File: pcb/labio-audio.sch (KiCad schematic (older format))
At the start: 27 parts

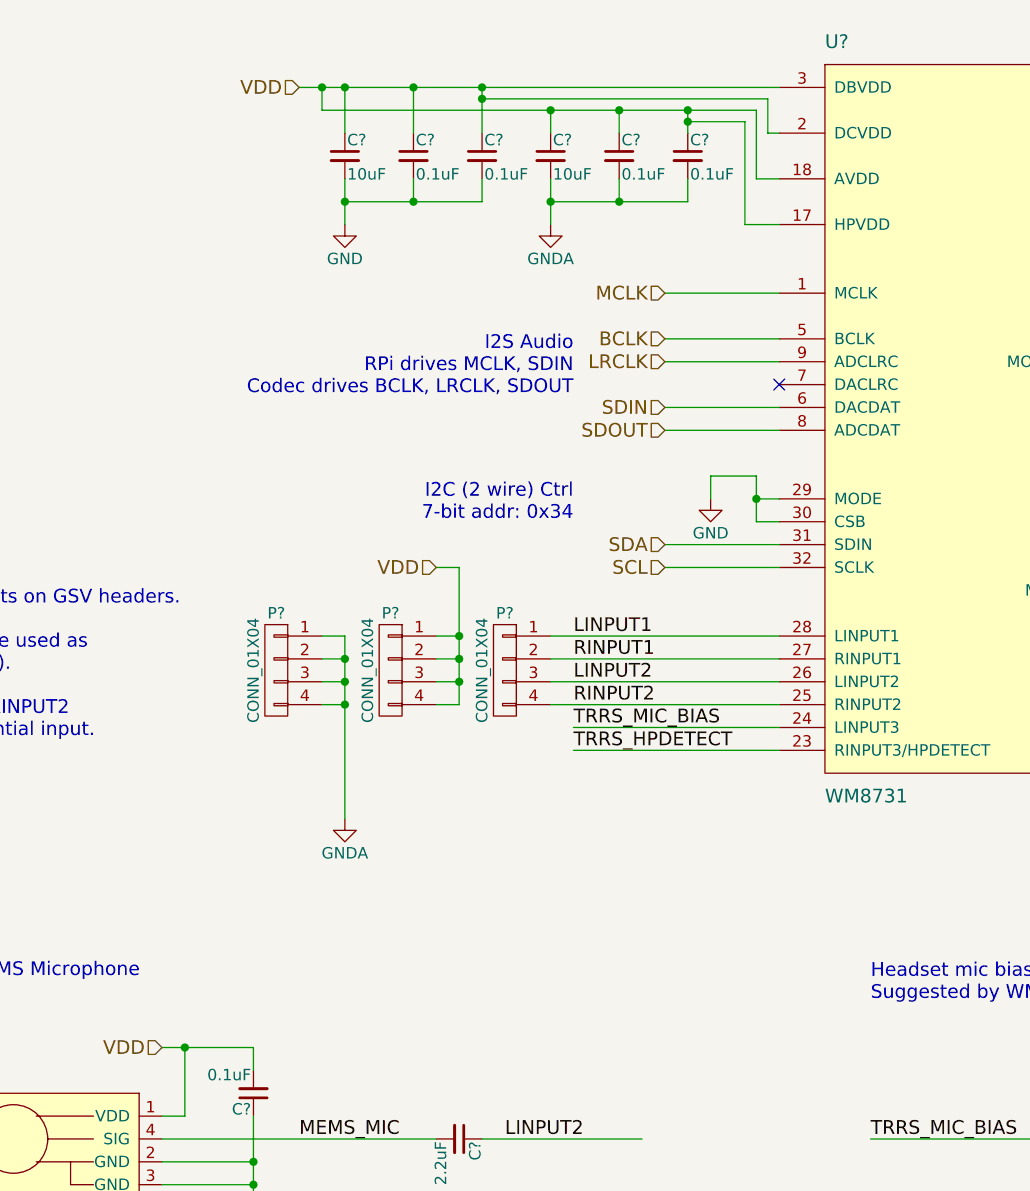
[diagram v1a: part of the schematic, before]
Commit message: add imu sensors, make top level connections
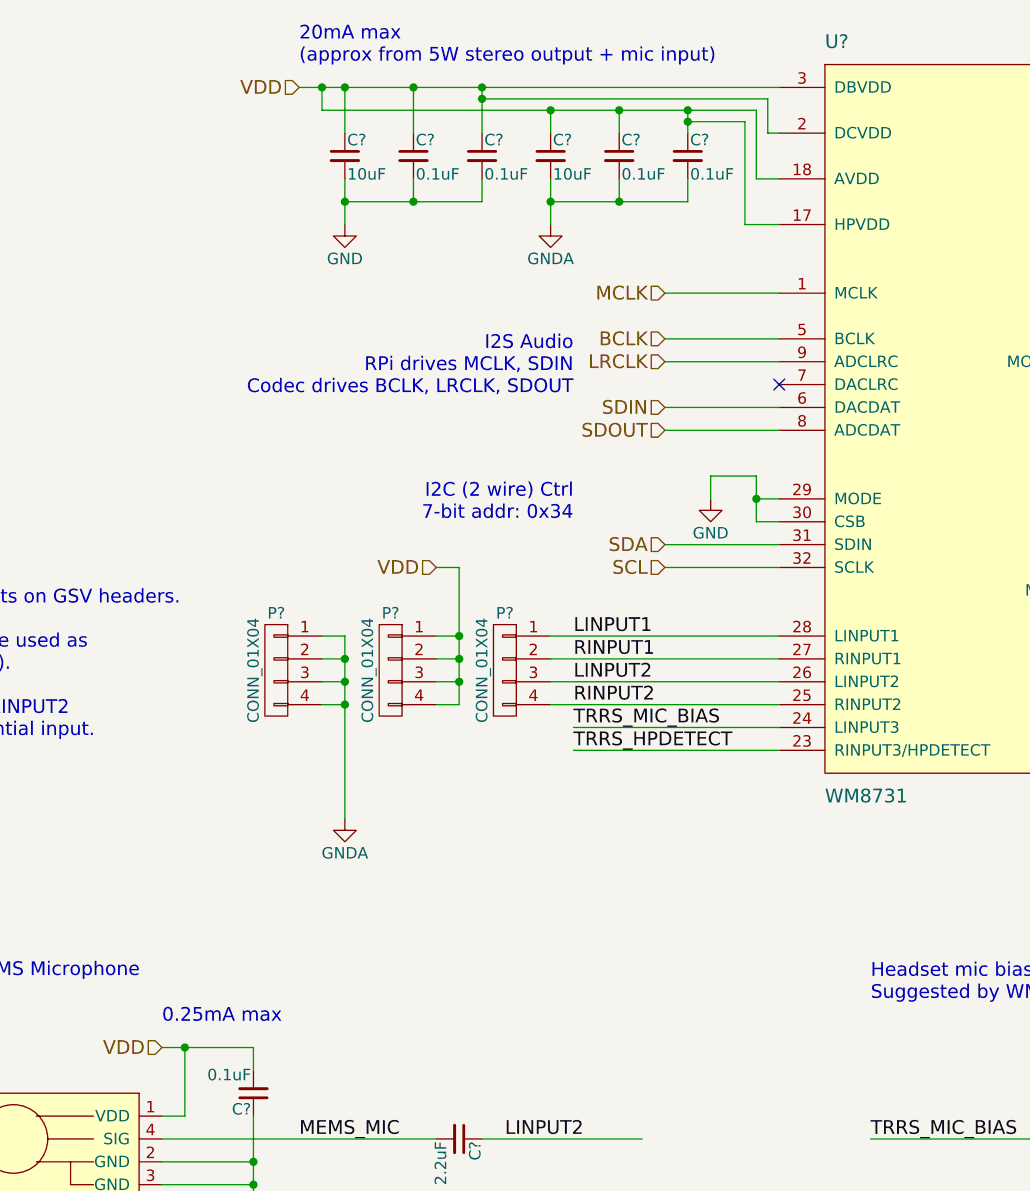
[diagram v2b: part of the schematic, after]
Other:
- note added: "0.25mA max"
- note added: "20mA max\n(approx from 5W stereo output + mic input)"
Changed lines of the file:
@@
 $Descr A4 11693 8268
 encoding utf-8
-Sheet 4 8
+Sheet 4 7
 Title ""
 Date ""
@@
 Text Notes 5700 5000 0    60   ~ 0
 Headset mic bias\nSuggested by WM8750BL datasheet (pg. 56).
+Text Notes 2600 5100 0    60   ~ 0
+0.25mA max
+Text Notes 3200 900  0    60   ~ 0
+20mA max\n(approx from 5W stereo output + mic input)
 $EndSCHEMATC

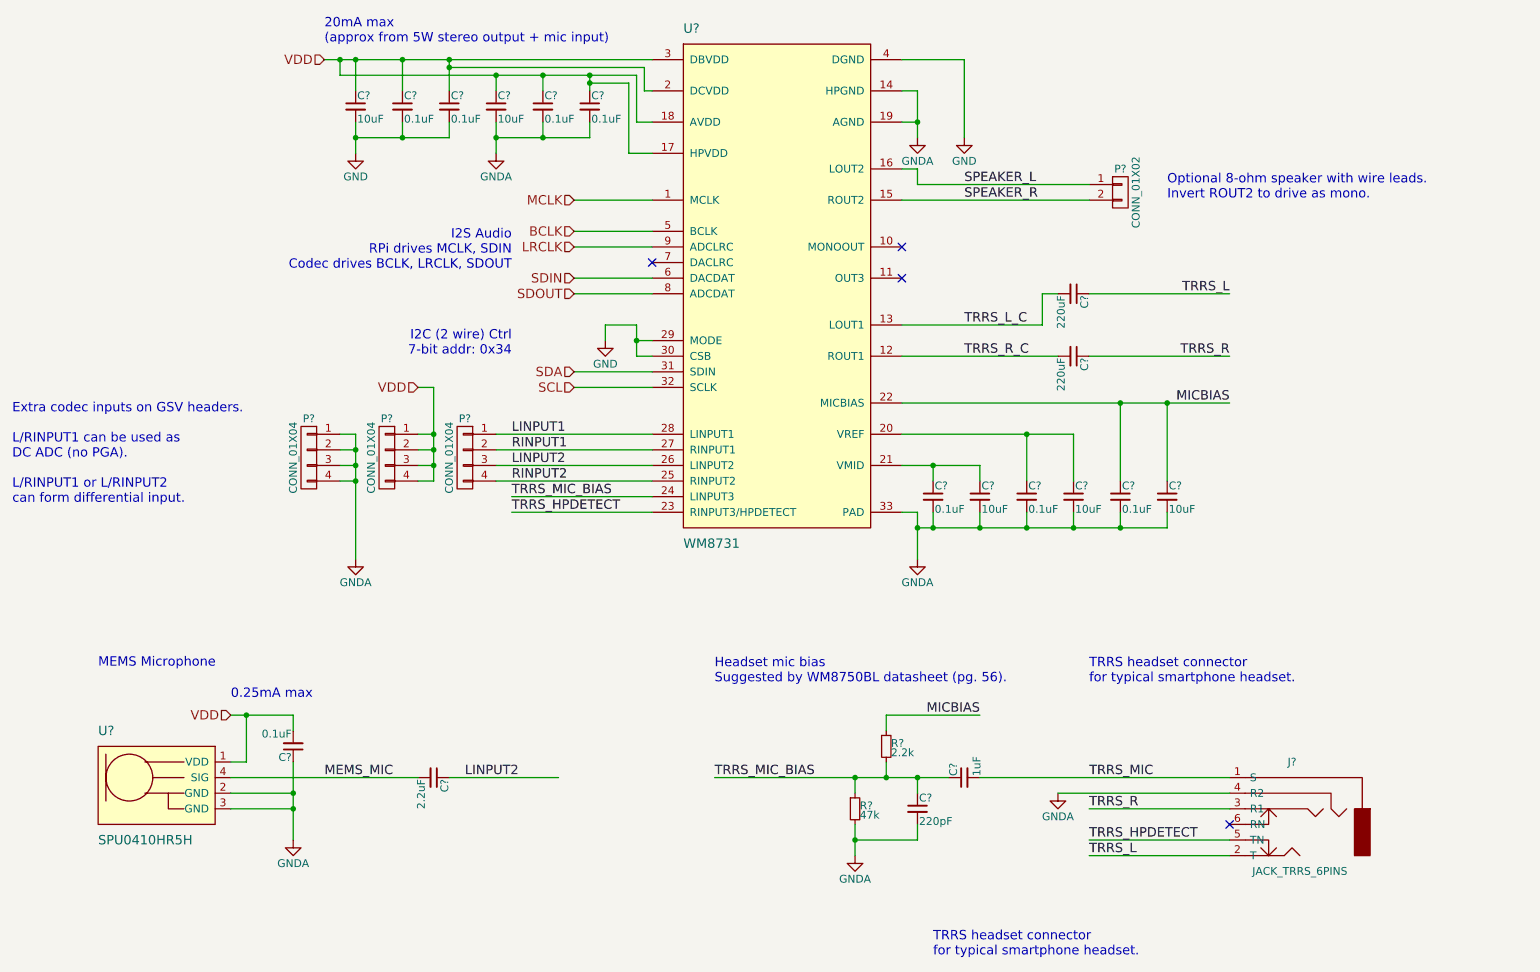
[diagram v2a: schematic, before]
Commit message: finish rpi to module connections
* use dip switches to disable/configure blocks
* add light sensor
* fix motor controller sense resistors
* fix overused jtag probe pins
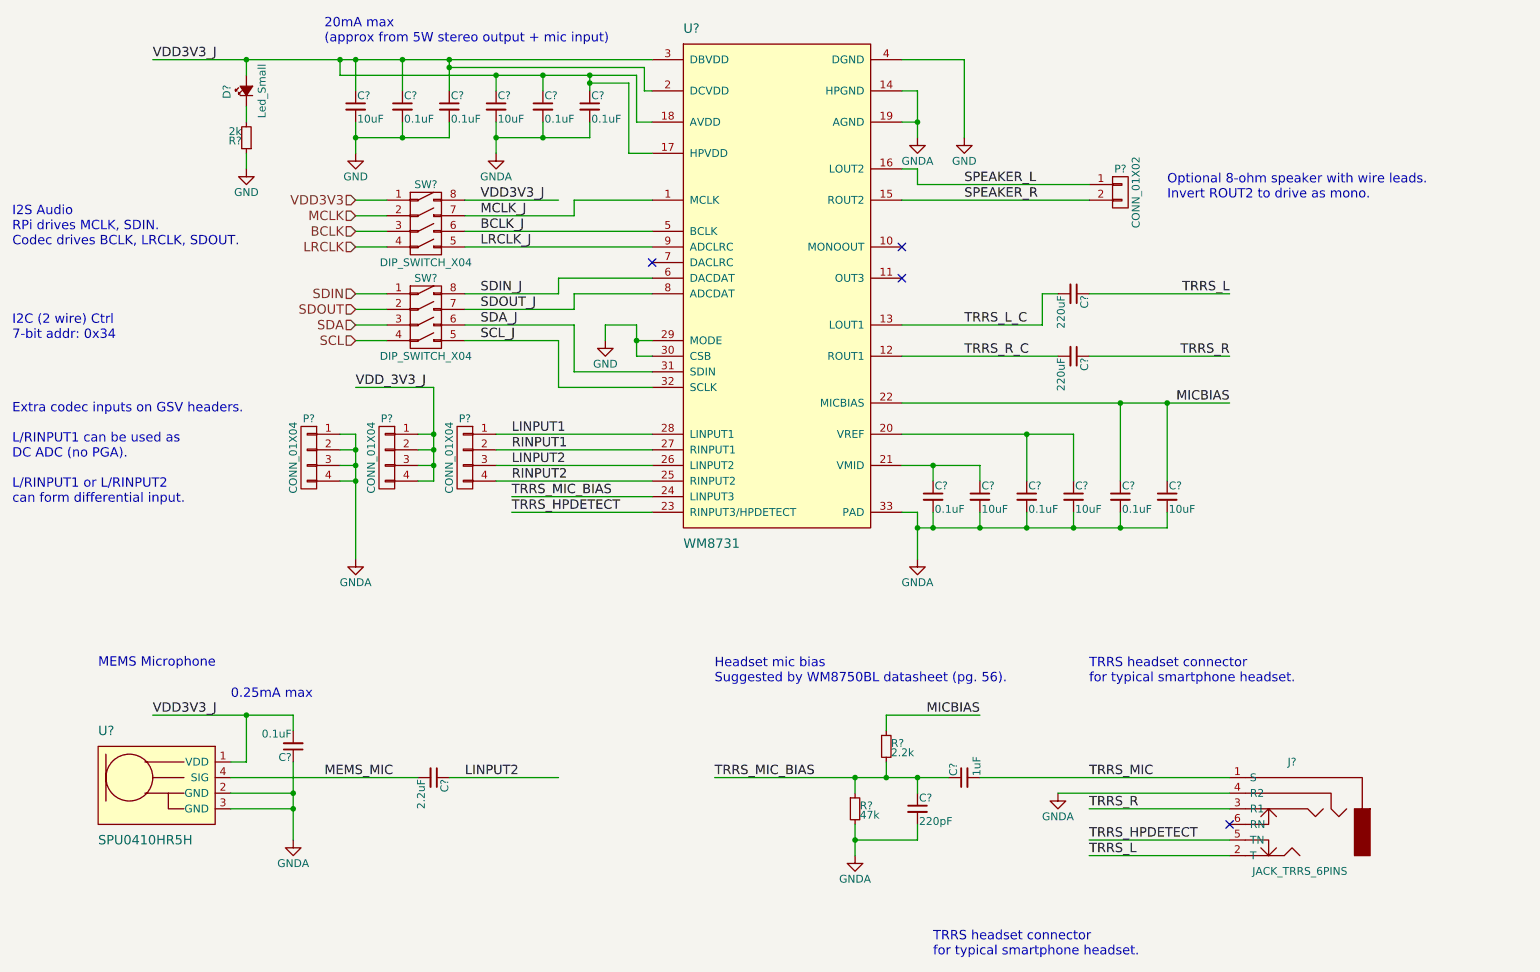
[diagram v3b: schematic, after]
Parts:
- added D?: Led_Small, symbol Led_Small
- added R?: 2k, symbol R_Small
- added SW? (x2): DIP_SWITCH_X04, symbol DIP_SWITCH_X04
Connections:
- net BCLK: now also SW?.3 (3A); no longer U?.5 (BCLK)
- net GND: now also R?.1
- net LRCLK: now also SW?.4 (4A); no longer U?.9 (ADCLRC)
- net MCLK: now also SW?.2 (2A); no longer U?.1 (MCLK)
- net SCL: now also SW?.4 (4A); no longer U?.32 (SCLK)
- net SDA: now also SW?.3 (3A); no longer U?.31 (SDIN)
- net SDIN: now also SW?.1 (1A); no longer U?.6 (DACDAT)
- net SDOUT: now also SW?.2 (2A); no longer U?.8 (ADCDAT)
- net VDD renamed VDD3V3_J
- net VDD3V3_J: now also D?.2 (A), SW?.8 (1B); no longer P?.1 (P1), P?.2 (P2), P?.3 (P3), P?.4 (P4)
- new net: D?.1 (K), R?.2
- new net BCLK_J: SW?.6 (3B), U?.5 (BCLK)
- new net LRCLK_J: SW?.5 (4B), U?.9 (ADCLRC)
- new net MCLK_J: SW?.7 (2A), U?.1 (MCLK)
- new net SCL_J: SW?.5 (4B), U?.32 (SCLK)
- new net SDA_J: SW?.6 (3B), U?.31 (SDIN)
- new net SDIN_J: SW?.8 (1B), U?.6 (DACDAT)
- new net SDOUT_J: SW?.7 (2A), U?.8 (ADCDAT)
- new net VDD3V3: SW?.1 (1A)
- new net VDD_3V3_J: P?.1 (P1), P?.2 (P2), P?.3 (P3), P?.4 (P4)
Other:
- note added: "I2S Audio\nRPi drives MCLK, SDIN.\nCodec drives BCLK, LRCLK, SDOUT."
- note removed: "I2S Audio\nRPi drives MCLK, SDIN\nCodec drives BCLK, LRCLK, SDOUT"

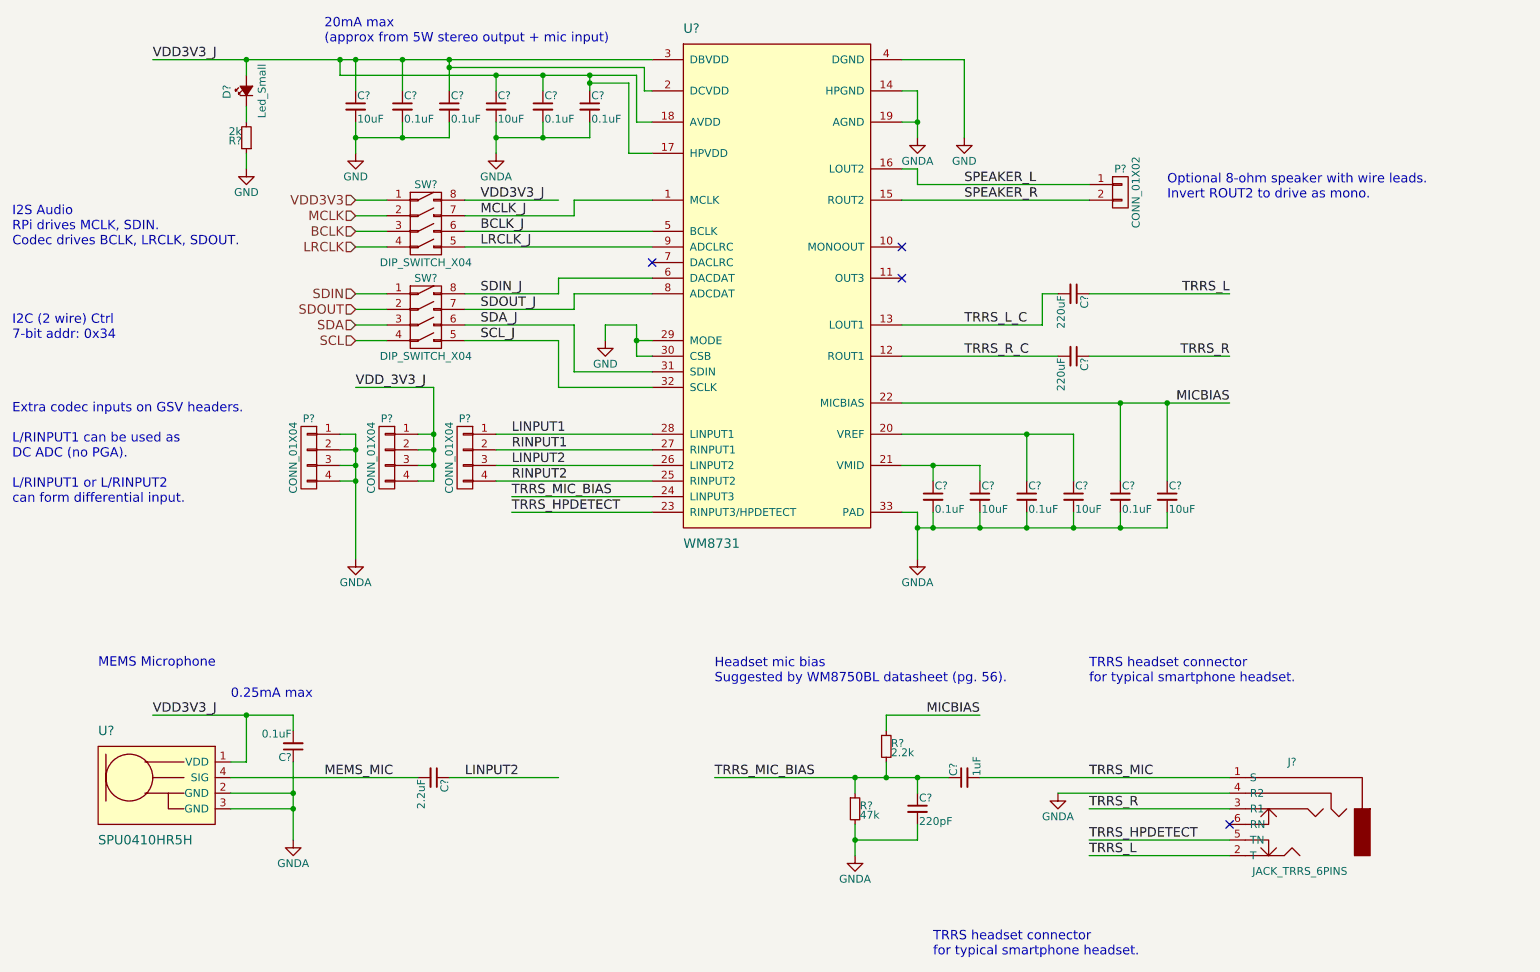
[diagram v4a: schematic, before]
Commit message: make extra footprints. start floorplan. fix display nets. add power expansion header.
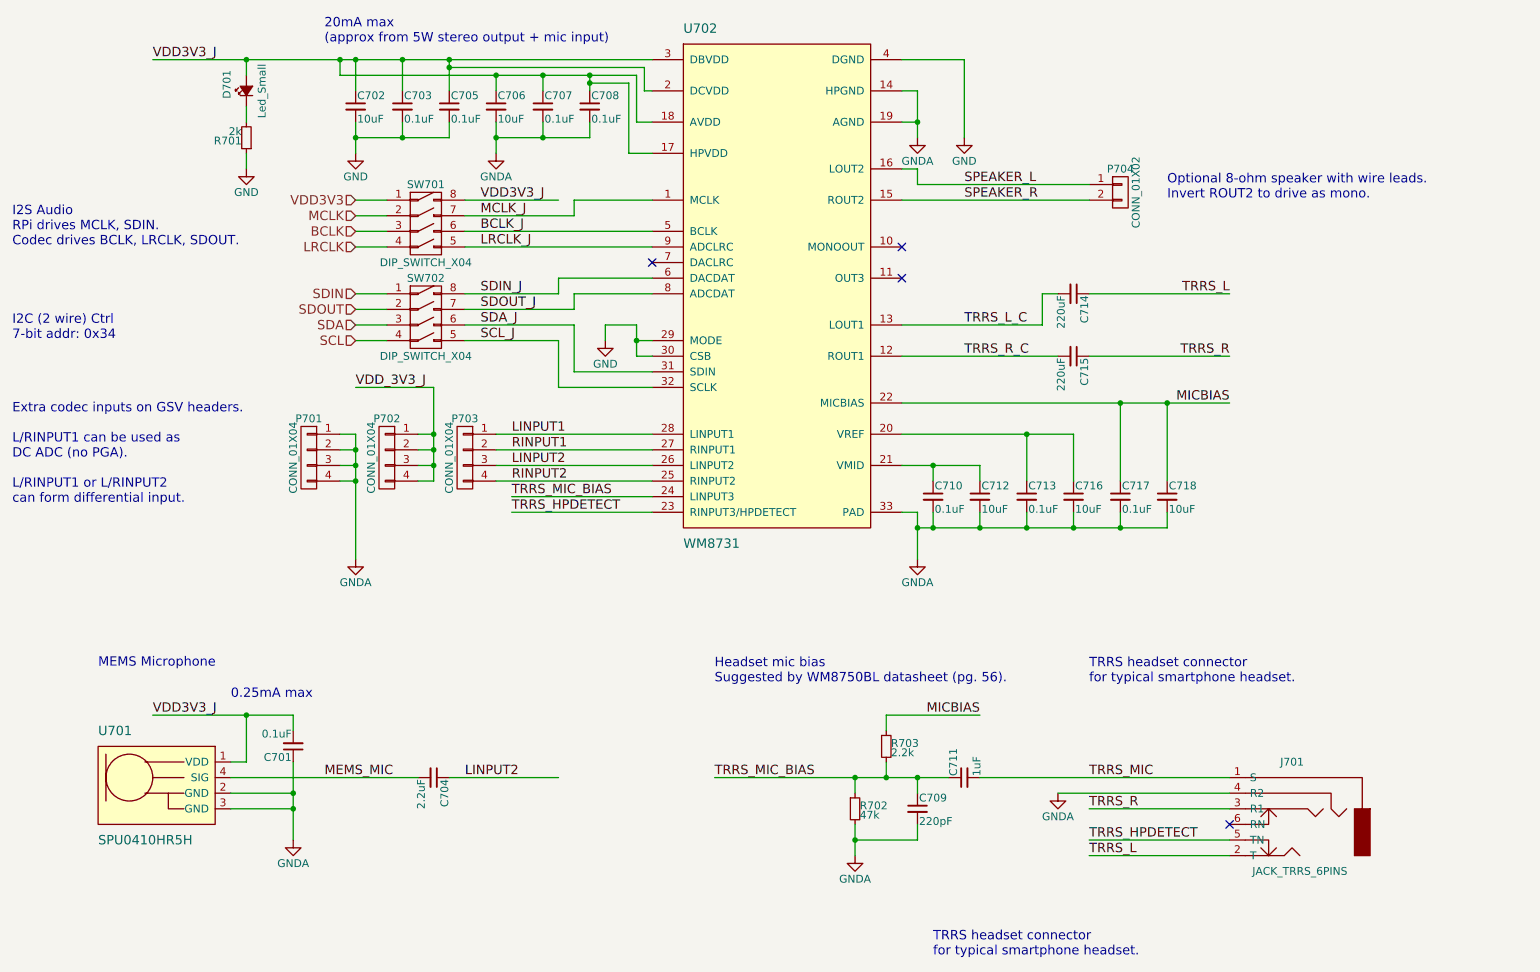
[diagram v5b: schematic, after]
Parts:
- C701, C703, C704, C705, C707, C708, C709, C710, C711, C713, C714, C715, C717: renamed from C?; footprint (none) -> Capacitors_SMD:C_0603
- C702, C706, C712, C716, C718: renamed from C?; footprint (none) -> Capacitors_Tantalum_SMD:TantalC_SizeA_EIA-3216_Wave
- D701: renamed from D?; footprint (none) -> LEDs:LED-0603
- J701: renamed from J?; footprint (none) -> labio-special:3.5mm-Jack-CUI-SJ-4351X
- P701, P702, P703: renamed from P?; footprint (none) -> Pin_Headers:Pin_Header_Straight_1x04
- P704: renamed from P?; footprint (none) -> Pin_Headers:Pin_Header_Straight_1x02
- R701, R702, R703: renamed from R?; footprint (none) -> Resistors_SMD:R_0603
- SW701, SW702: renamed from SW?; footprint (none) -> labio-special:DIP-8_W7.62mm_SMT
- U701: renamed from U?; footprint (none) -> labio-special:SPU0410HR5H
- U702: renamed from U?; footprint (none) -> Housings_DFN_QFN:QFN-32-1EP_5x5mm_Pitch0.5mm
